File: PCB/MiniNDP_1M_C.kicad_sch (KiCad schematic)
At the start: 15 parts, among them J1 Conn_02x20_Odd_Even, U1 AS6C8008_TSOPII, U2 HC238, U3 4040, U4 FCT841

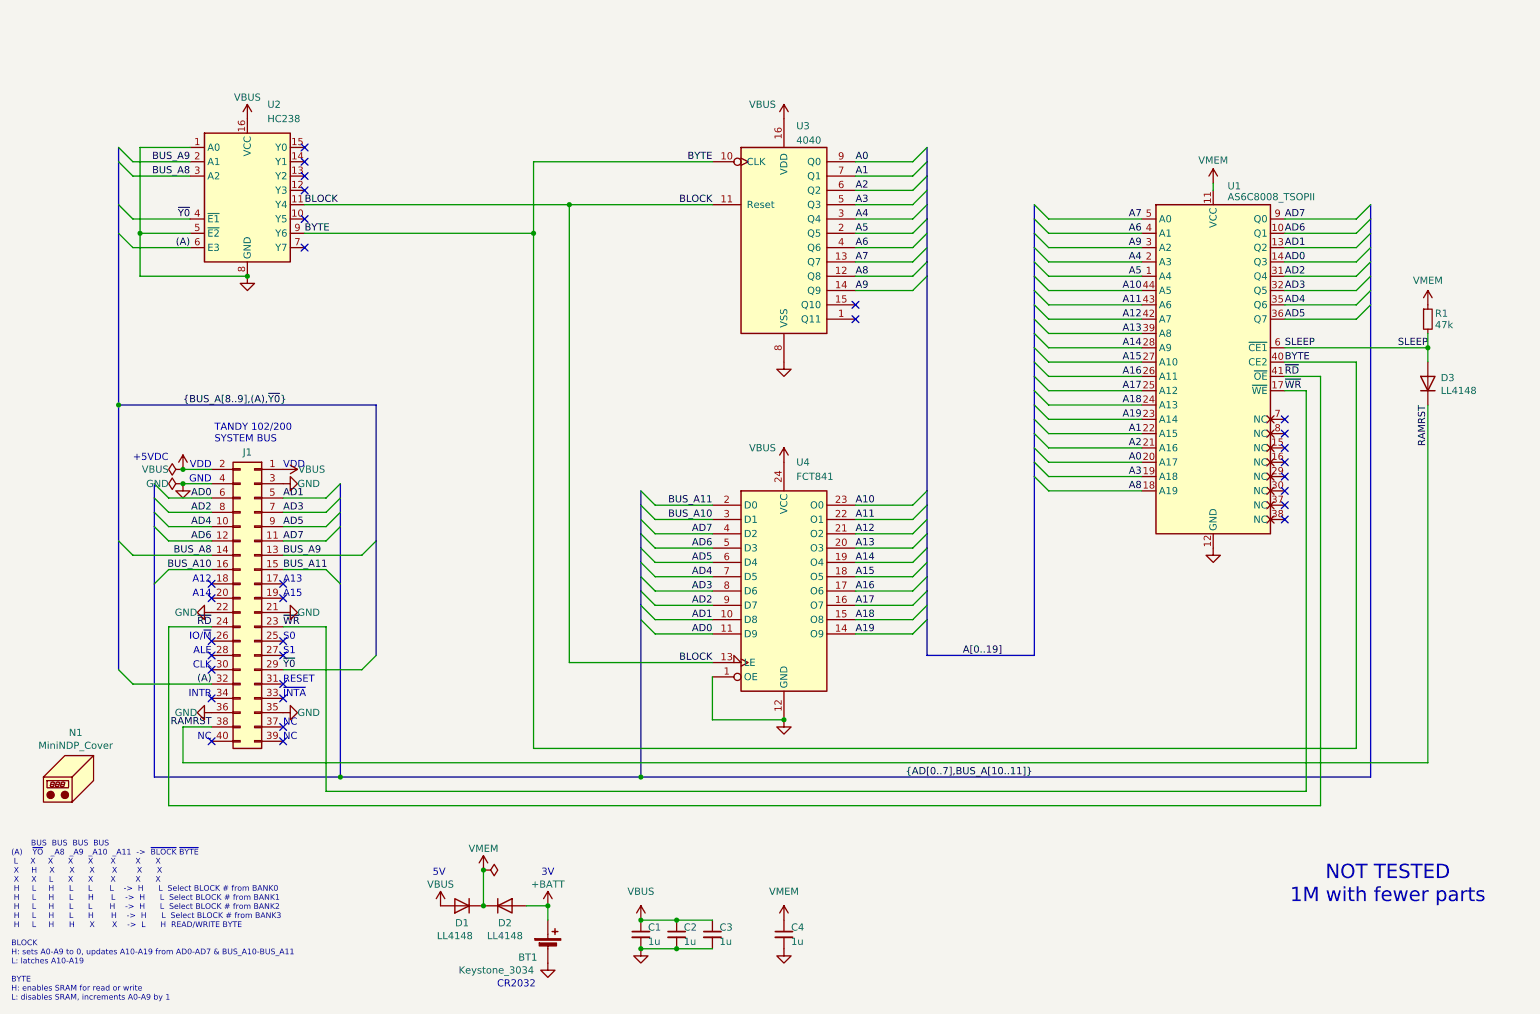
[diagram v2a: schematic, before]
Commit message: 512_F 1M_C remove ramrst diode, 1u caps
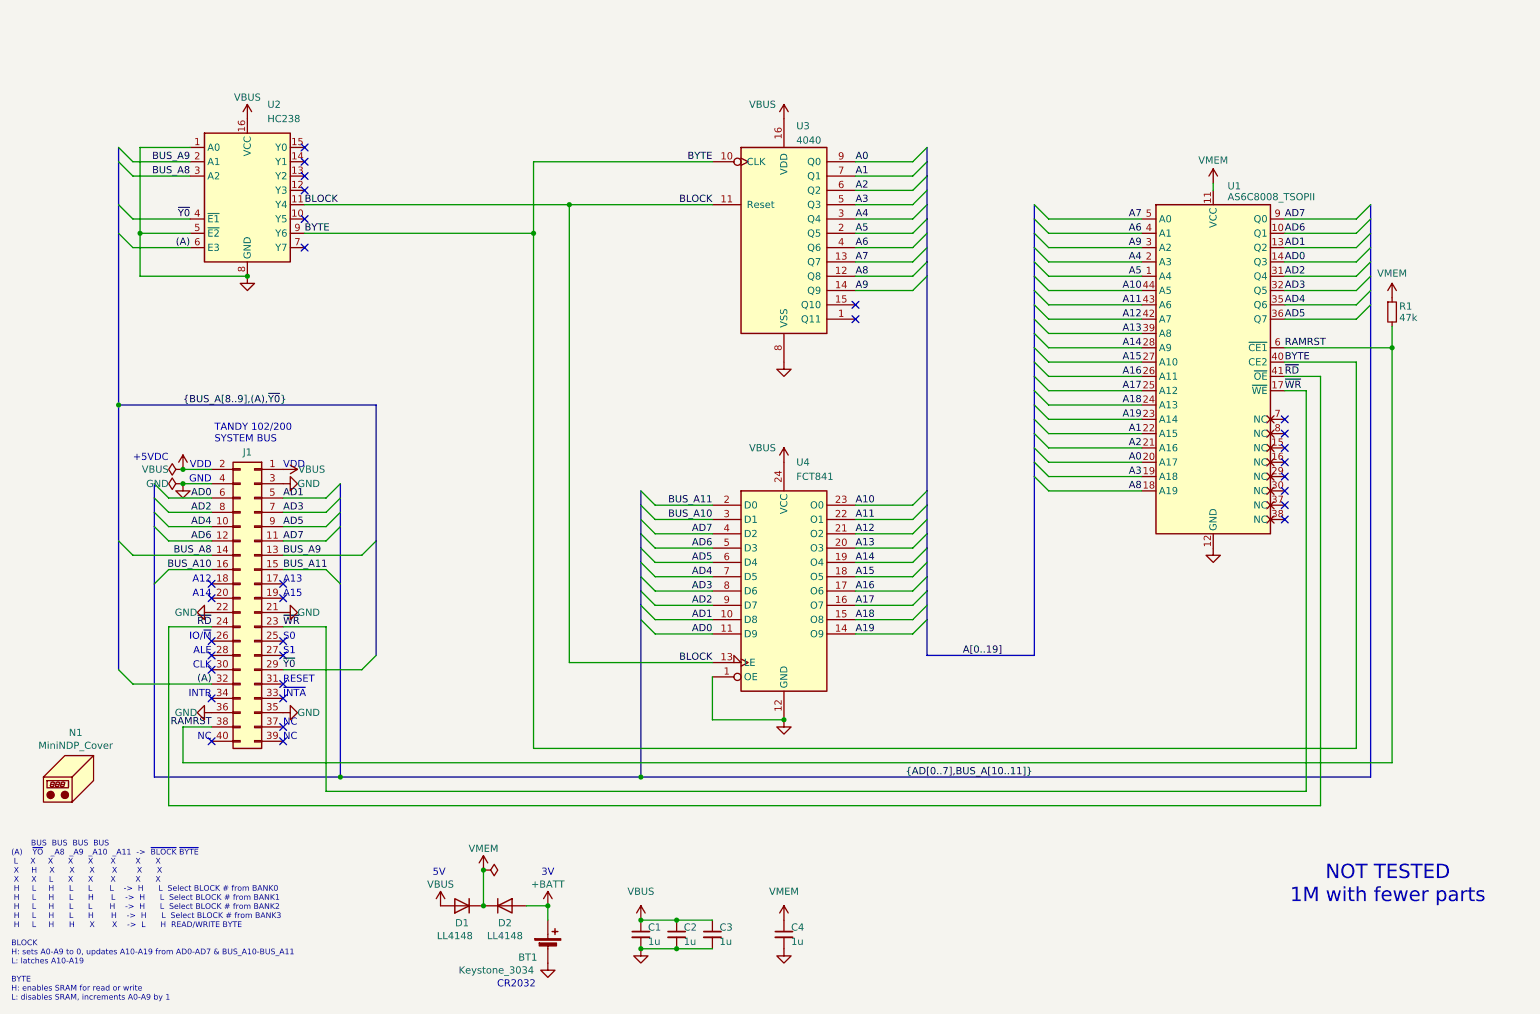
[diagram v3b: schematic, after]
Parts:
- removed D3: LL4148, 000_LOCAL:D_MiniMELF, symbol 000_LOCAL:LL4148
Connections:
- net SLEEP is gone; now on net RAMRST: R1.2, U1.6 (~{CE1})
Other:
- moved on the sheet: R1
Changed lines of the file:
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@@
 	)
 	(junction
-		(at 266.7 78.74)
+		(at 260.35 78.74)
 		(diameter 0)
 		(color 0 0 0 0)
@@
 	(wire
 		(pts
-			(xy 266.7 76.2) (xy 266.7 78.74)
+			(xy 260.35 74.93) (xy 260.35 78.74)
 		)
 		(stroke
@@
 	(wire
 		(pts
-			(xy 266.7 88.9) (xy 266.7 152.4)
+			(xy 260.35 78.74) (xy 260.35 152.4)
 		)
 		(stroke
@@
 	(wire
 		(pts
-			(xy 266.7 78.74) (xy 266.7 81.28)
-		)
-		(stroke
-			(width 0)
-			(type default)
-		)
-	)
-	(wire
-		(pts
 			(xy 199.39 104.14) (xy 215.9 104.14)
 		)
@@
 	(wire
 		(pts
-			(xy 241.3 78.74) (xy 266.7 78.74)
+			(xy 241.3 78.74) (xy 260.35 78.74)
 		)
 		(stroke
@@
 	(wire
 		(pts
-			(xy 45.72 152.4) (xy 266.7 152.4)
+			(xy 45.72 152.4) (xy 260.35 152.4)
 		)
 		(stroke
@@
 		)
 	)
-	(label "SLEEP"
-		(at 266.7 78.74 180)
-		(fields_autoplaced yes)
-		(effects
-			(font
-				(size 1.27 1.27)
-			)
-			(justify right bottom)
-		)
-	)
 	(label "A13"
 		(at 215.9 76.2 180)
@@
 	)
 	(label "RAMRST"
-		(at 266.7 88.9 270)
+		(at 241.3 78.74 0)
 		(fields_autoplaced yes)
 		(effects
@@
 				(size 1.27 1.27)
 			)
-			(justify right bottom)
+			(justify left bottom)
 		)
 	)
@@
 		)
 	)
-	(label "SLEEP"
-		(at 241.3 78.74 0)
-		(fields_autoplaced yes)
-		(effects
-			(font
-				(size 1.27 1.27)
-			)
-			(justify left bottom)
-		)
-	)
 	(label "A4"
 		(at 215.9 63.5 180)
@@
 	)
 	(symbol
-		(lib_id "000_LOCAL:LL4148")
-		(at 266.7 85.09 90)
-		(unit 1)
-		(exclude_from_sim no)
-		(in_bom yes)
-		(on_board yes)
-		(dnp no)
-		(property "Reference" "D3"
-			(at 268.986 84.074 90)
-			(effects
-				(font
-					(size 1.27 1.27)
-				)
-				(justify right)
-			)
-		)
-		(property "Value" "LL4148"
-			(at 268.986 86.36 90)
-			(effects
-				(font
-					(size 1.27 1.27)
-				)
-				(justify right)
-			)
-		)
-		(property "Footprint" "000_LOCAL:D_MiniMELF"
-			(at 266.7 85.09 0)
-			(effects
-				(font
-					(size 1.27 1.27)
-				)
-				(hide yes)
-			)
-		)
-		(property "Datasheet" "datasheets/ll4148.pdf"
-			(at 266.7 85.09 0)
-			(effects
-				(font
-					(size 1.27 1.27)
-				)
-				(hide yes)
-			)
-		)
-		(property "Description" "50V 1A General Purpose Rectifier Diode"
-			(at 266.7 85.09 0)
-			(effects
-				(font
-					(size 1.27 1.27)
-				)
-				(hide yes)
-			)
-		)
-		(property "MPN" "FDLL4148"
-			(at 266.7 85.09 0)
-			(effects
-				(font
-					(size 1.27 1.27)
-				)
-				(hide yes)
-			)
-		)
-		(pin "1"
-		)
-		(pin "2"
-		)
-		(instances
-			(project "MiniNDP_1M_C"
-				(path "/f15c2929-5cf4-4b4e-965d-148e1bec8a42"
-					(reference "D3")
-					(unit 1)
-				)
-			)
-		)
-	)
-	(symbol
 		(lib_id "power:PWR_FLAG")
 		(at 45.72 102.87 90)
@@
 	(symbol
 		(lib_id "power:VMEM")
-		(at 266.7 71.12 0)
+		(at 260.35 69.85 0)
 		(unit 1)
 		(exclude_from_sim no)
@@
 		(dnp no)
 		(property "Reference" "#PWR014"
-			(at 266.7 74.93 0)
+			(at 260.35 73.66 0)
 			(effects
 				(font
@@
 		)
 		(property "Value" "VMEM"
-			(at 266.7 66.802 0)
+			(at 260.35 65.532 0)
 			(effects
 				(font
@@
 		)
 		(property "Footprint" ""
-			(at 266.7 71.12 0)
+			(at 260.35 69.85 0)
 			(effects
 				(font
@@
 		)
 		(property "Datasheet" ""
-			(at 266.7 71.12 0)
+			(at 260.35 69.85 0)
 			(effects
 				(font
@@
 		)
 		(property "Description" "Power symbol creates a global label with name \"VMEM\""
-			(at 266.7 71.12 0)
+			(at 260.35 69.85 0)
 			(effects
 				(font
@@
 	(symbol
 		(lib_id "000_LOCAL:R")
-		(at 266.7 73.66 0)
+		(at 260.35 72.39 0)
 		(unit 1)
 		(exclude_from_sim no)
@@
 		(dnp no)
 		(property "Reference" "R1"
-			(at 267.97 72.644 0)
+			(at 261.62 71.374 0)
 			(effects
 				(font
@@
 		)
 		(property "Value" "47k"
-			(at 267.97 74.676 0)
+			(at 261.62 73.406 0)
 			(effects
 				(font
@@
 		)
 		(property "Footprint" "000_LOCAL:R_0805"
-			(at 266.7 73.66 0)
+			(at 260.35 72.39 0)
 			(effects
 				(font
@@
 		)
 		(property "Datasheet" "datasheets/sei-rmcf_rmcp.pdf"
-			(at 266.7 73.66 0)
+			(at 260.35 72.39 0)
 			(effects
 				(font
@@
 		)
 		(property "Description" "RES 47K OHM 1% 1/8W 0805"
-			(at 266.7 73.66 0)
+			(at 260.35 72.39 0)
 			(effects
 				(font
@@
 		)
 		(property "MPN" "RMCF0805FT47K0"
-			(at 266.7 73.66 0)
+			(at 260.35 72.39 0)
 			(effects
 				(font

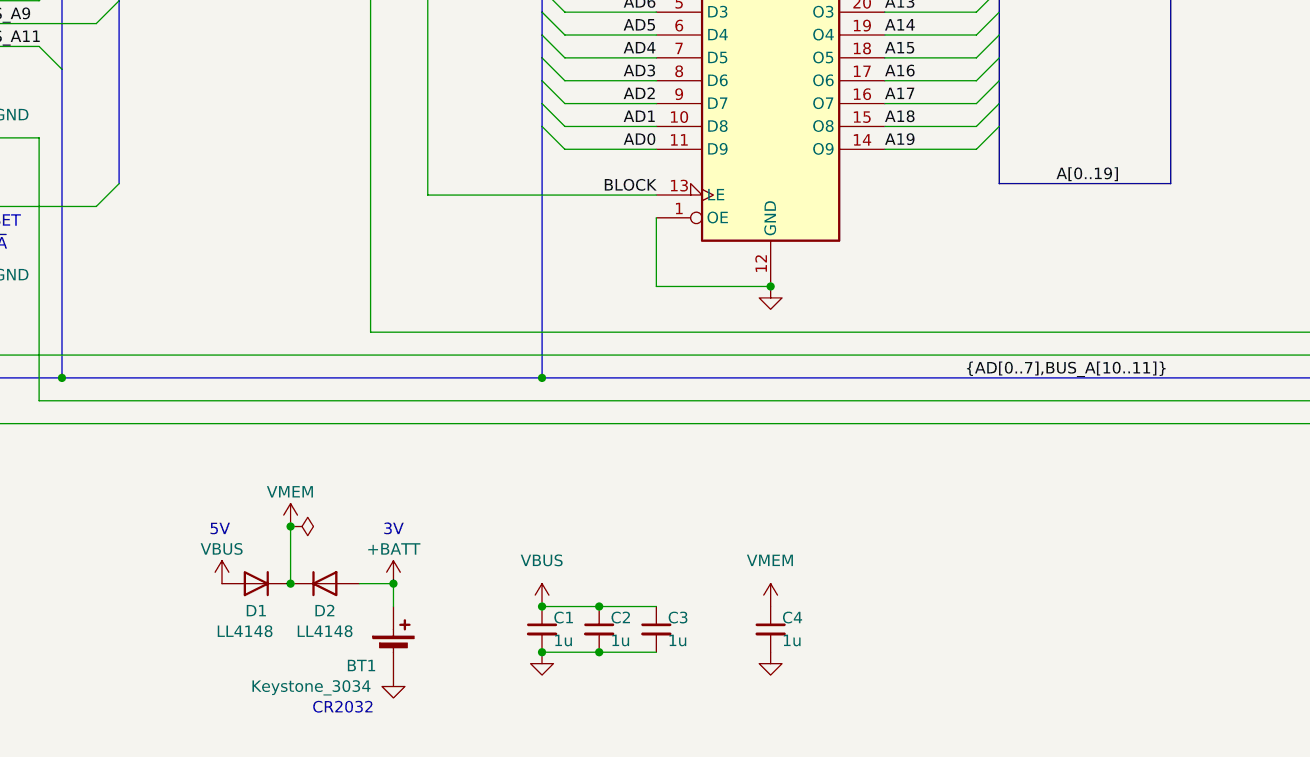
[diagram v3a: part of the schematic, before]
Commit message: easy boards add 47u cap, remove ramrst diode
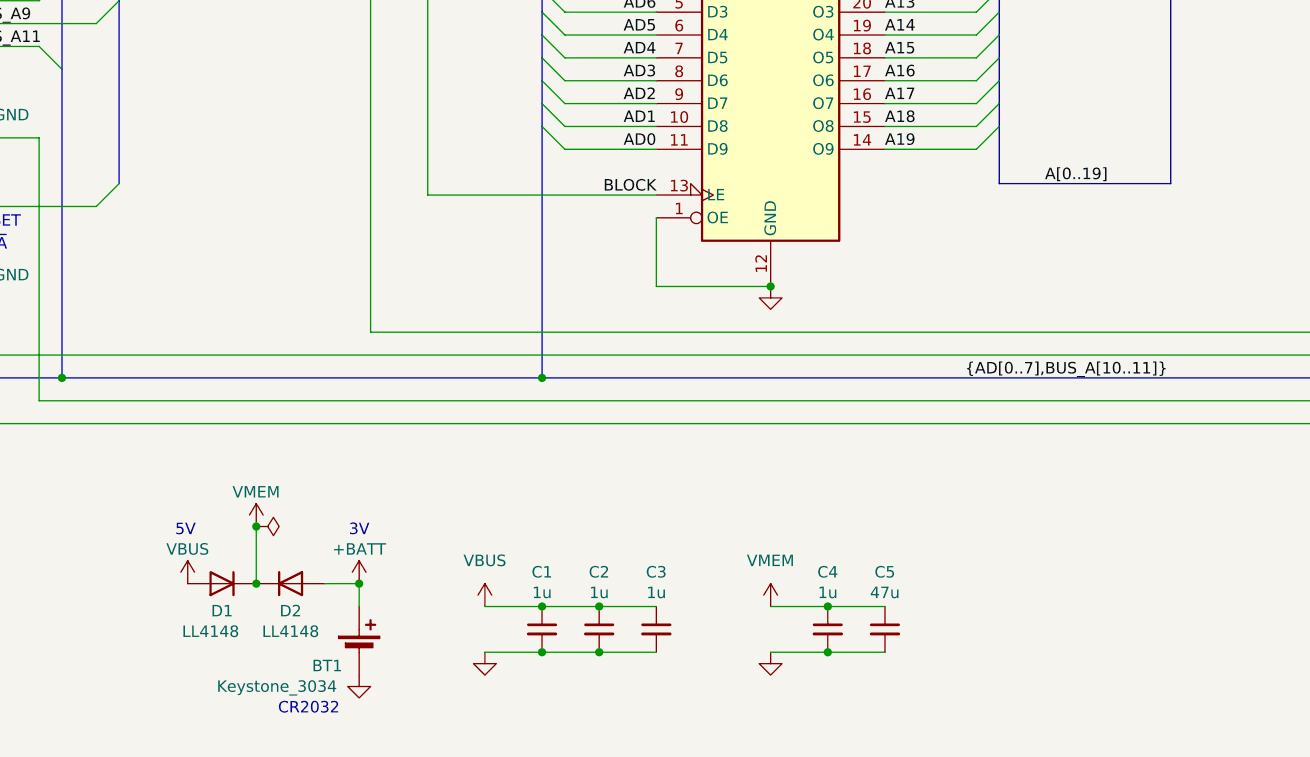
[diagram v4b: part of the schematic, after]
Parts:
- added C5: 47u, 000_LOCAL:C_1206, symbol 000_LOCAL:C
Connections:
- net GND: now also C5.2
- net VMEM: now also C5.1
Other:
- moved on the sheet: BT1, C4, D1, D2

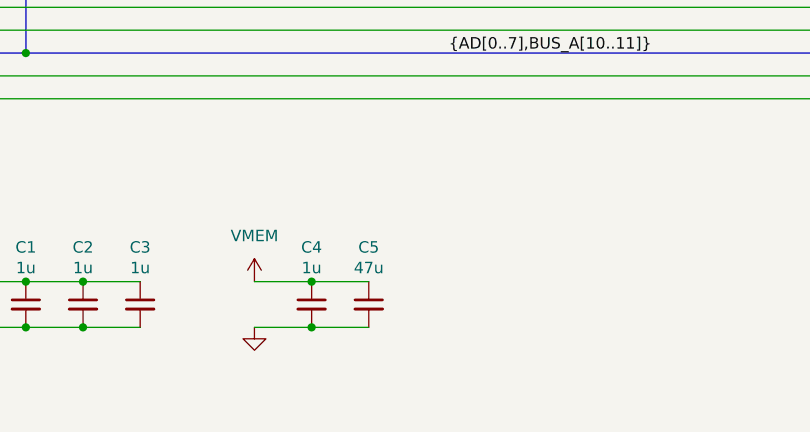
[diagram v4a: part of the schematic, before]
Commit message: 1M_C move passives around
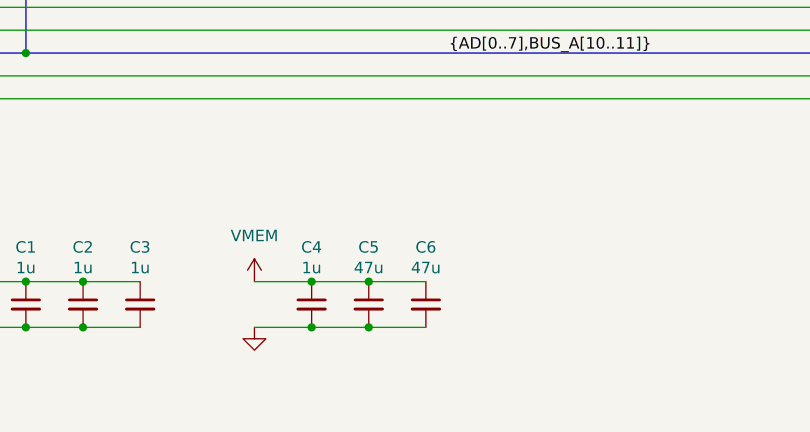
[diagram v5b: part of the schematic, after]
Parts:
- added C6: 47u, 000_LOCAL:C_1206, symbol 000_LOCAL:C
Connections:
- net GND: now also C6.2
- net VMEM: now also C6.1
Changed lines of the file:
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@@
 	(title_block
 		(title "MiniNDP 1M")
-		(date "2024-11-28")
-		(rev "C02")
+		(date "2024-12-10")
+		(rev "C03")
 		(company "Brian K. White - b.kenyon.w@gmail.com")
 		(comment 1 "github.com/bkw777/NODE_DATAPAC")
@@
 	)
 	(junction
+		(at 165.1 180.34)
+		(diameter 0)
+		(color 0 0 0 0)
+	)
+	(junction
 		(at 95.25 171.45)
 		(diameter 0)
@@
 	)
 	(junction
+		(at 165.1 185.42)
+		(diameter 0)
+		(color 0 0 0 0)
+	)
+	(junction
 		(at 127 154.94)
 		(diameter 0)
@@
 		)
 	)
+	(wire
+		(pts
+			(xy 165.1 185.42) (xy 171.45 185.42)
+		)
+		(stroke
+			(width 0)
+			(type default)
+		)
+	)
 	(bus
 		(pts
@@
 		)
 	)
+	(wire
+		(pts
+			(xy 165.1 180.34) (xy 171.45 180.34)
+		)
+		(stroke
+			(width 0)
+			(type default)
+		)
+	)
 	(bus
 		(pts
@@
 					(unit 1)
 				)
+			)
+		)
+	)
+	(symbol
+		(lib_id "000_LOCAL:C")
+		(at 171.45 182.88 0)
+		(unit 1)
+		(exclude_from_sim no)
+		(in_bom yes)
+		(on_board yes)
+		(dnp no)
+		(property "Reference" "C6"
+			(at 171.45 176.53 0)
+			(effects
+				(font
+					(size 1.27 1.27)
+				)
+			)
+		)
+		(property "Value" "47u"
+			(at 171.45 178.816 0)
+			(effects
+				(font
+					(size 1.27 1.27)
+				)
+			)
+		)
+		(property "Footprint" "000_LOCAL:C_1206"
+			(at 171.45 182.88 0)
+			(effects
+				(font
+					(size 1.27 1.27)
+				)
+				(hide yes)
+			)
+		)
+		(property "Datasheet" "datasheets/TDK_MLCC_Cxxxx.pdf"
+			(at 171.45 182.88 0)
+			(effects
+				(font
+					(size 1.27 1.27)
+				)
+				(hide yes)
+			)
+		)
+		(property "Description" "CAP CER 47UF 25V X5R 1206"
+			(at 171.45 182.88 0)
+			(effects
+				(font
+					(size 1.27 1.27)
+				)
+				(hide yes)
+			)
+		)
+		(property "MPN" "C3216X5R1E476M160DC"
+			(at 171.45 182.88 0)
+			(effects
+				(font
+					(size 1.27 1.27)
+				)
+				(hide yes)
+			)
+		)
+		(pin "2"
+		)
+		(pin "1"
+		)
+		(instances
+			(project "MiniNDP_1M_C06"
+				(path "/f15c2929-5cf4-4b4e-965d-148e1bec8a42"
+					(reference "C6")
+					(unit 1)
+				)
